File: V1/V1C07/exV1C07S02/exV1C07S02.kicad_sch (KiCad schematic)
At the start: 5 parts

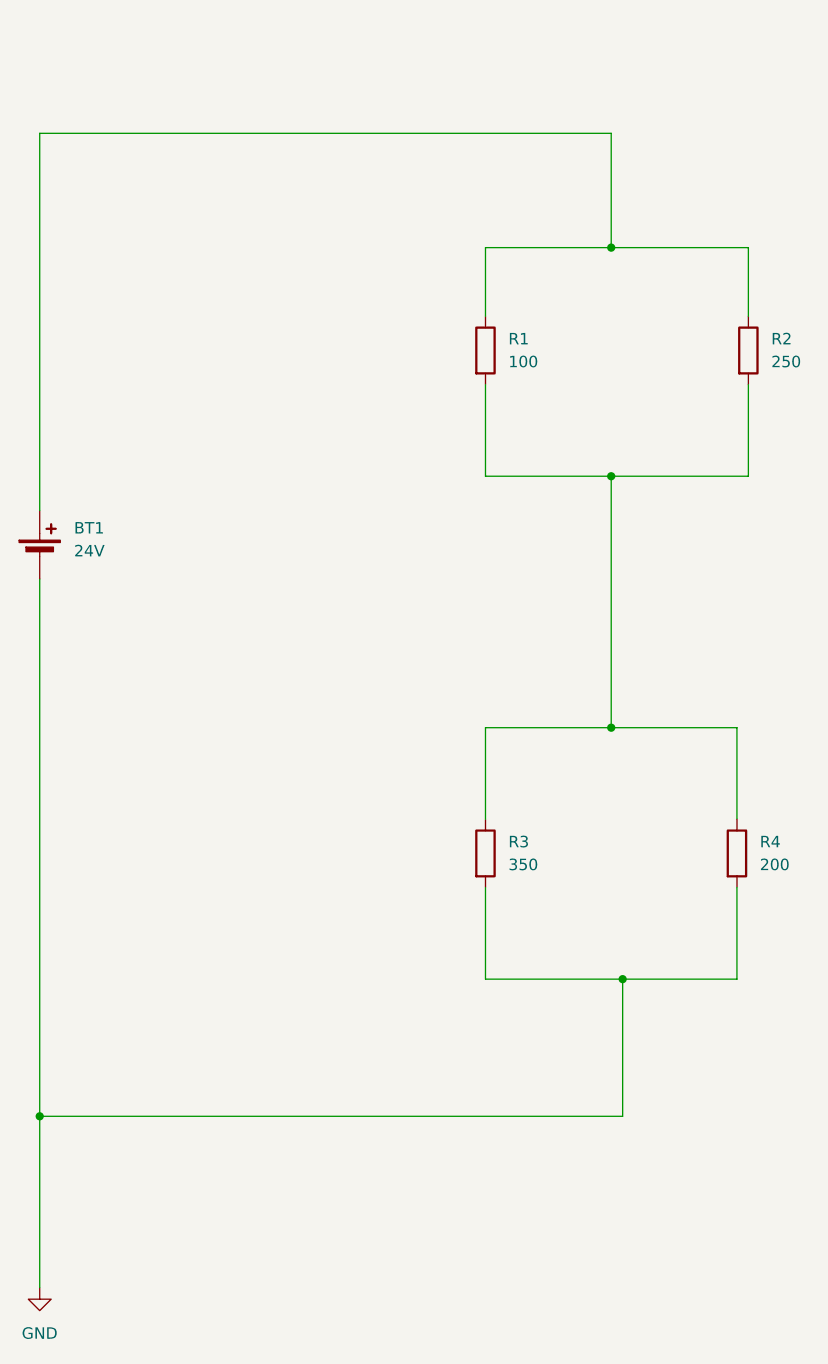
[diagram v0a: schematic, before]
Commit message: update V1 C05 C06 C07
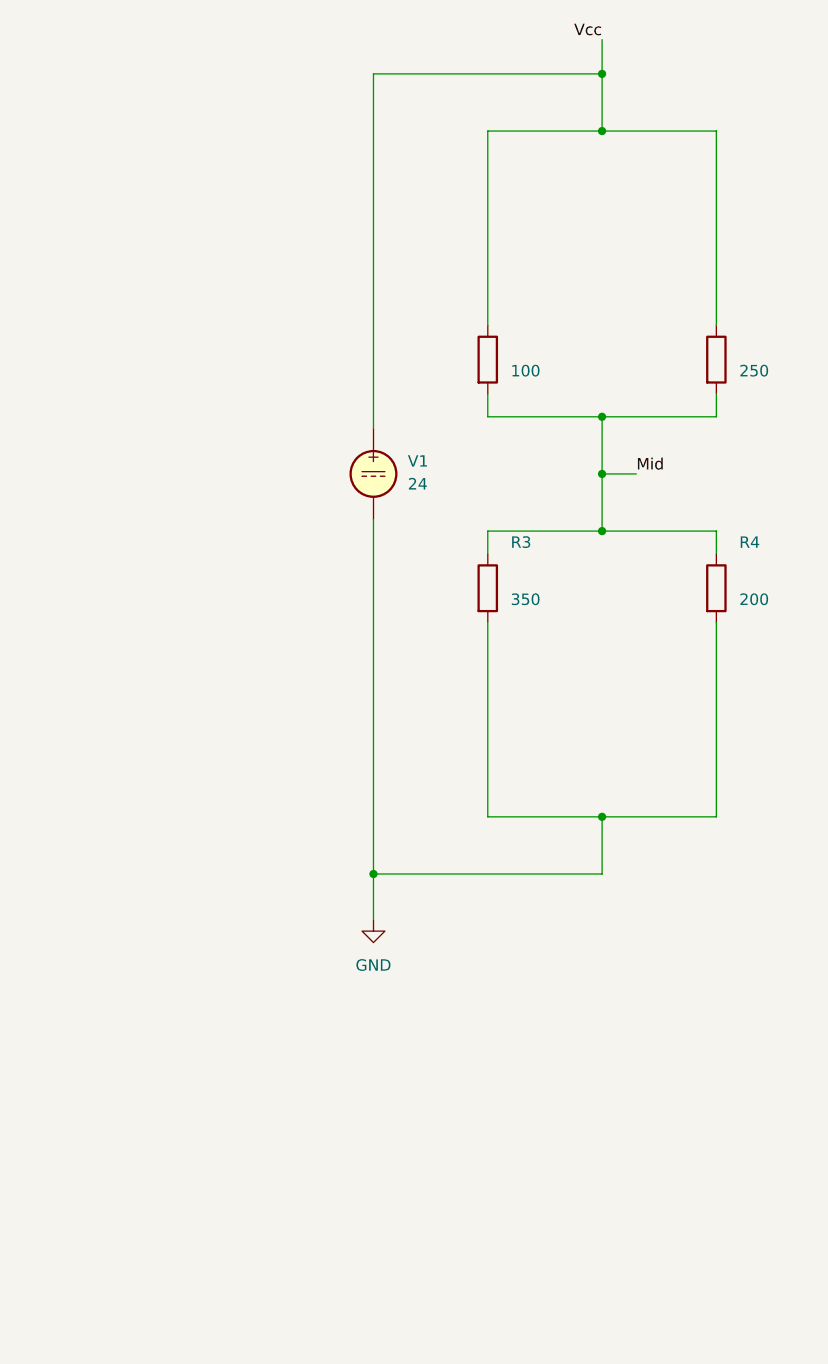
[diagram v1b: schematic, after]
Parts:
- removed BT1: 24V, symbol Device:Battery_Cell
- added V1: 24, symbol Simulation_SPICE:VDC
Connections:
- net GND: now also V1.2
- net Mid: now reaches R1.2, R2.2, R3.1, R4.1
- net Vcc: now reaches R1.1, R2.1
- net Vcc: now also V1.1
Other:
- moved on the sheet: R3, R4
